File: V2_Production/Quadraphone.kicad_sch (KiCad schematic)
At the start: 40 parts, among them J1 Conn_01x10_Male, J2 Conn_01x10_Male, J3 Conn_01x10_Male, J4 Conn_01x10_Male, J5 Eurorack_10_pin_power, Q1 MMBT3904, U1 AMS1117-5.0, U14 LM4040DBZ-2.5, U3 MCP6002, U4 LM4040DBZ-5, U5 MCP6004, U8 74LV4066PW

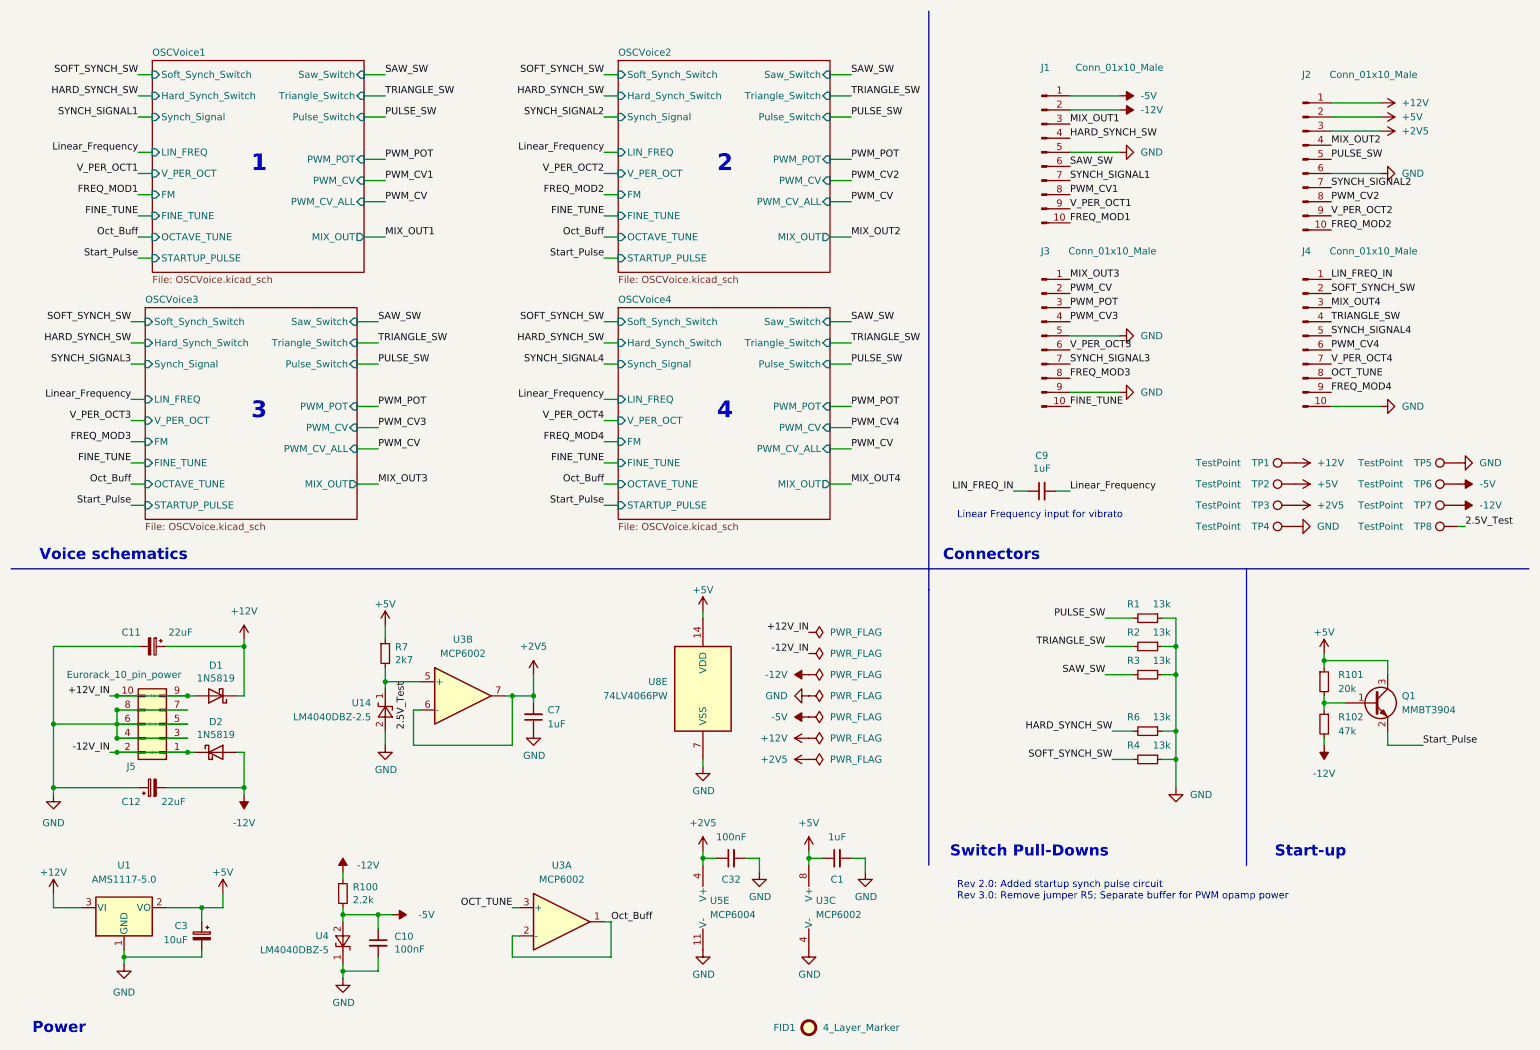
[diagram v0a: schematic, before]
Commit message: Started Rev 3 with buffered octave control
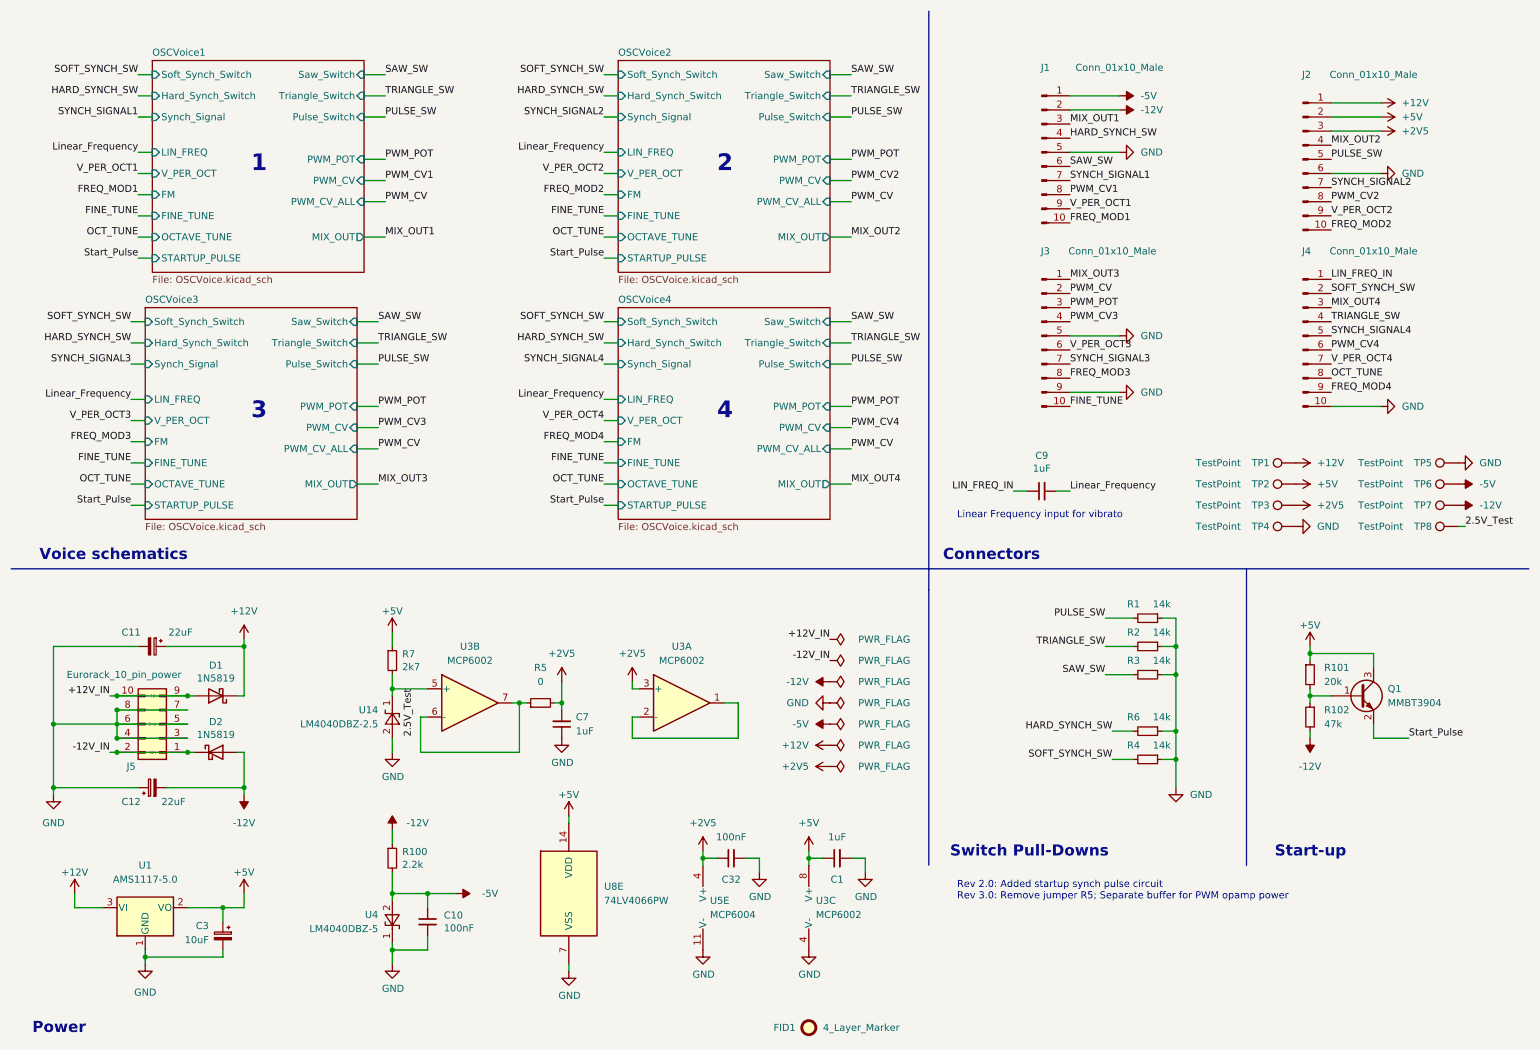
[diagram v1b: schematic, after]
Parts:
- added R5: 0, Resistor_SMD:R_0603_1608Metric, symbol Device:R_Small
- R1, R2, R3, R4, R6: value 13k -> 14k
- U3: footprint Package_SO:SOIC-8_3.9x4.9mm_P1.27mm -> Package_SO:MSOP-8_3x3mm_P0.65mm
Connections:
- net +2V5: now also U3.3 (+), R5.2; no longer U3.6 (-), U3.7
- net OCT_TUNE: no longer U3.3 (+)
- net Oct_Buff: no longer names the net of U3.1, U3.2 (-)
- new net: R5.1, U3.6 (-), U3.7
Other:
- moved on the sheet: C10, C3, C7, Q1, R100, R101, R102, R7, U1, U14, U3B, U4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
